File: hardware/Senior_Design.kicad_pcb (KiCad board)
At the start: 4 copper layers, 144 x 146 mm, 162 parts, among them IC301 TLV61220DBVT, J201 Conn_ARM_JTAG_SWD_10, J301 Barrel_Jack_Switch, J302 Conn_01x03, J401 Conn_ARM_JTAG_SWD_10, J601 USB_C_Receptacle_USB2.0_16P, J701 J0011D21BNL, Q301 CSD87503Q3E, Q302 CSD87503Q3E, Q303 Q_NMOS, SW201 SW_Push, SW401 SW_Push, U201 EFR32FG28A122F1024GM48-A, U202 USBLC6-2P6, U203 USBLC6-2P6, U301 TPS63020DSJR, U302 BQ25798RQMR, U401 USBLC6-2P6, U402 USBLC6-2P6, U403 BDE-MB1352P71UA32, U501 BME688, U502 USBLC6-2P6, U602 CDSOT236-0504C, U603 CP2102N-A02-GQFN20, U701 W5500, U702 USBLC6-2P6, U703 USBLC6-2P6, X201 HF_Crystal, Y201 LF_Crystal, Y701 25MHz

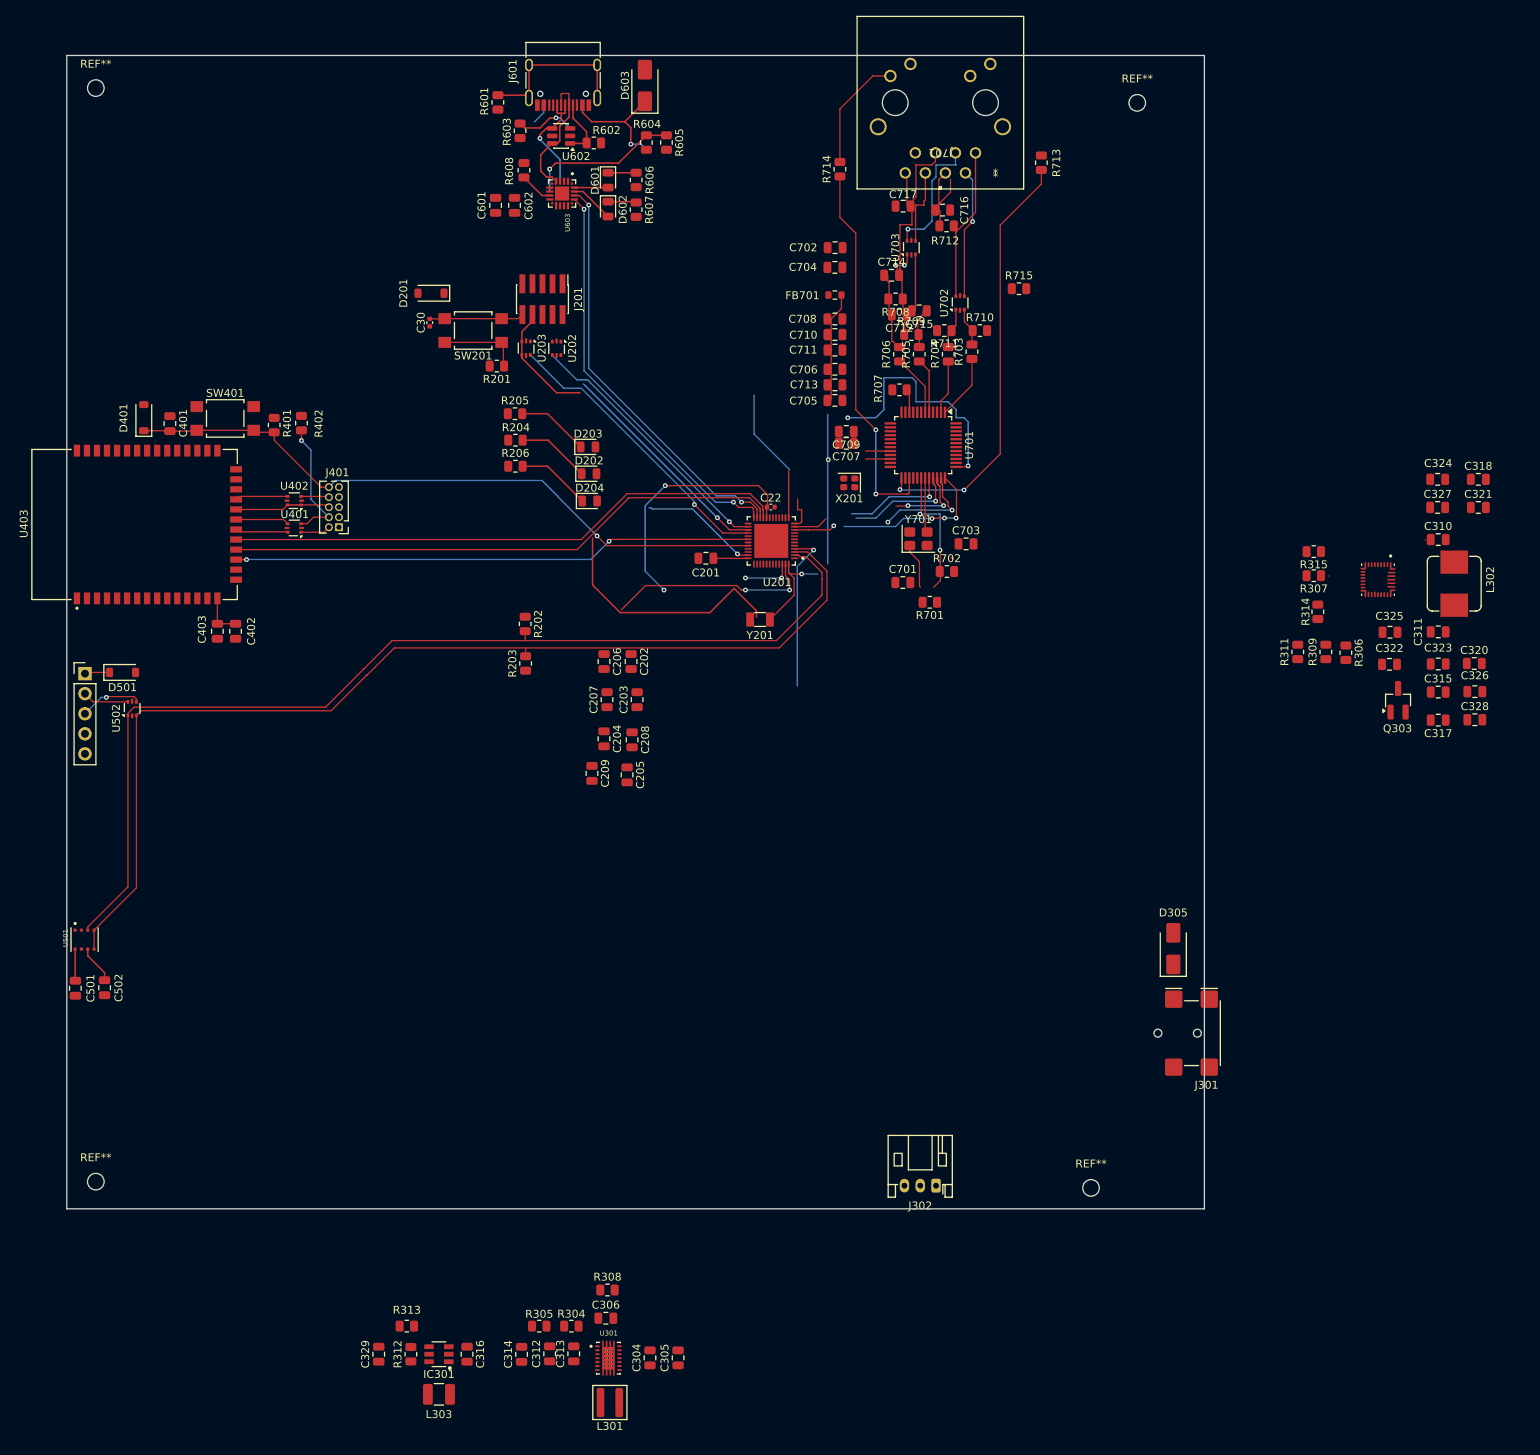
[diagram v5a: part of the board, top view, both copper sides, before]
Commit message: updated footprints
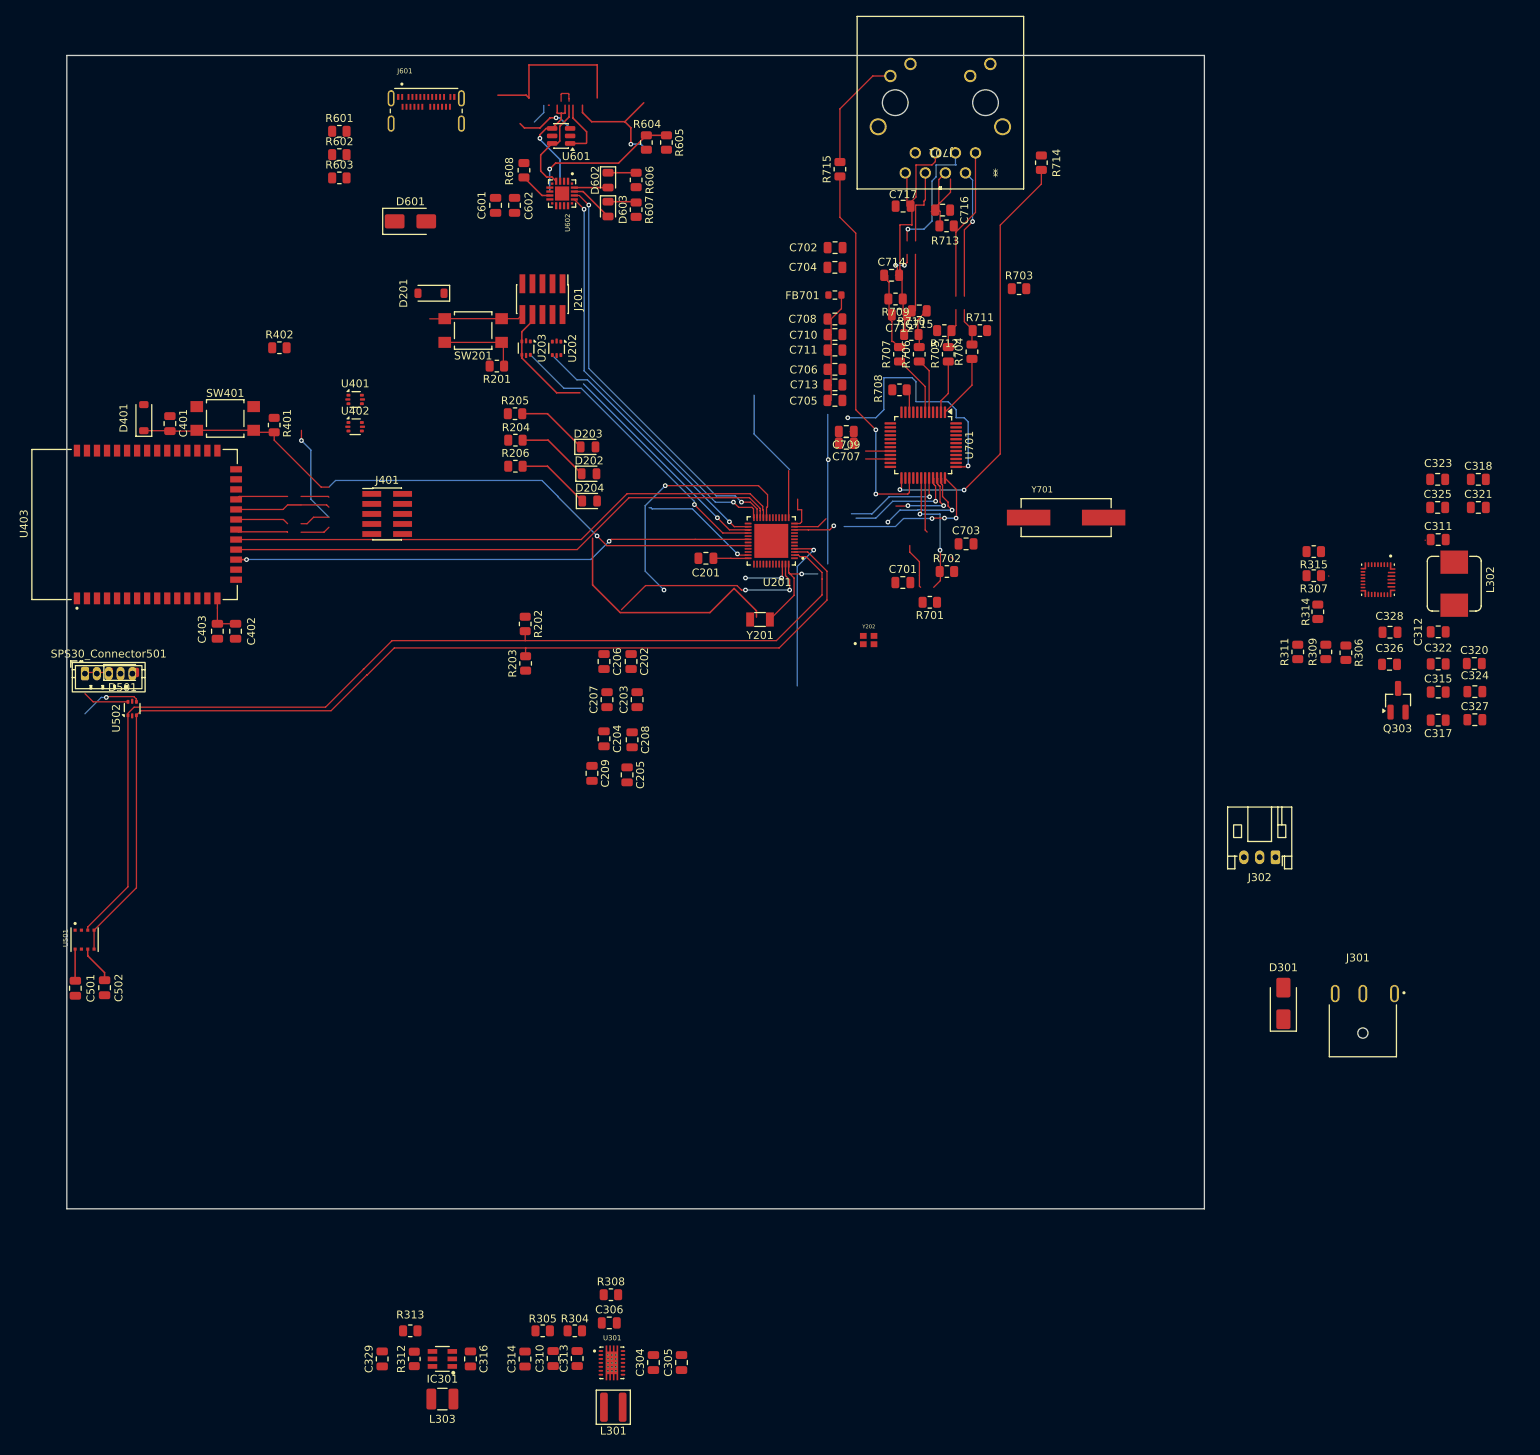
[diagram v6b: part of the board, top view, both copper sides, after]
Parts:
- removed C22: 120pF, Capacitor_SMD:C_0402_1005Metric
- removed C30: 100nF, Capacitor_SMD:C_0402_1005Metric
- removed the D603 at (96.2, 23.8)
- removed REF** (x4): MountingHole_2.1mm, MountingHole:MountingHole_2.1mm
- removed U702, U703: USBLC6-2P6, Package_TO_SOT_SMD:SOT-666
- removed X201: HF_Crystal, Crystal:Crystal_SMD_2016-4Pin_2.0x1.6mm
- added D601: SMAJ12A, Diode_SMD:D_SMA, F.Cu at (66.5, 41.0)
- added Y202: ECS-390-CDX-1932, pyronet_footprints:XTAL_ECS-390-CDX-1932, F.Cu at (124.5, 94.0)
- J301: value Barrel_Jack_Switch -> 54-00125; footprint Connector_BarrelJack:BarrelJack_Wuerth_694102107102_1.0x3.9mm -> pyronet_footprints:TENSILITY_54-00125
- J401: footprint Connector_PinHeader_1.27mm:PinHeader_2x05_P1.27mm_Vertical -> Connector_PinHeader_1.27mm:PinHeader_2x05_P1.27mm_Vertical_SMD
- J601: value USB_C_Receptacle_USB2.0_16P -> 2305018-2; footprint Connector_USB:USB_C_Receptacle_HRO_TYPE-C-31-M-12 -> pyronet_footprints:TE_2305018-2
- R601: value 1M -> 5.1k
- R602: value 5.1k -> 1M
- SPS30_Connector501: footprint Connector_PinHeader_2.54mm:PinHeader_1x05_P2.54mm_Vertical -> Connector_JST:JST_ZH_B5B-ZR_1x05_P1.50mm_Vertical
- Y701: value 25MHz -> ECS-250-18-5PX-F-TR; footprint Crystal:Crystal_SMD_3225-4Pin_3.2x2.5mm -> pyronet_footprints:XTAL_ECS-250-18-5PX-F-TR
- moved J302 59.8 mm to (176.0, 121.5)
- moved R602 32.2 mm to (57.5, 32.5)
- moved R603 23.6 mm to (57.5, 35.5), turned to 0 degrees
- moved J301 22.8 mm to (187.1, 143.8), turned to 0 degrees
- moved R601 20.4 mm to (57.5, 29.6), turned to 0 degrees
- moved Y701 18.9 mm to (149.5, 78.5)
- moved J601 18.5 mm to (68.5, 28.9), turned to 0 degrees
- moved U401 18.0 mm to (59.5, 63.5), turned to 0 degrees
- moved D301 15.6 mm to (177.0, 140.0)
- moved U402 12.1 mm to (59.5, 67.0), turned to 0 degrees
- moved R402 9.94 mm to (49.9, 57.0), turned to 0 degrees
- moved J401 6.33 mm to (63.5, 78.0), turned to 0 degrees
- moved C304 0.74 mm to (97.3, 185.5)
- moved C305 0.74 mm to (100.8, 185.5)
- moved C314 0.74 mm to (81.0, 185.0)
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- renumbered C312 to C310, C310 to C311, C311 to C312, C323 to C322, C324 to C323, C326 to C324, C327 to C325, C322 to C326, C328 to C327, C325 to C328, D305 to D301, D601 to D602, D602 to D603, R715 to R703, R703 to R704, R704 to R705, R705 to R706, R706 to R707, R707 to R708, R708 to R709, R709 to R710, R710 to R711, R711 to R712, R712 to R713, R713 to R714, R714 to R715, U602 to U601, U603 to U602
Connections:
- R601 pad 1: Net-(J601-SHIELD) -> GND
- R601 pad 2: GND -> /USB-C/CC1
- R602 pad 1: /USB-C/CC1 -> Net-(J601-SHIELD-PadSH1)
- Y701 pad 2: GND -> Net-(U701-XO)
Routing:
- net +3.3V: track 0.74 -> 32.4 mm, vias 0 -> 2
- net /MCU/PAVDD: track 31.6 -> 0.00 mm, vias 2 -> 0
- net Net-(J601-SHIELD): track 21.1 -> 0.00 mm
- net (no net): track 96.2 -> 117.3 mm
- net /MCU/nRST: track 80.5 -> 82.4 mm
- net Net-(U2-~{RESET}): track 1.91 -> 0.00 mm

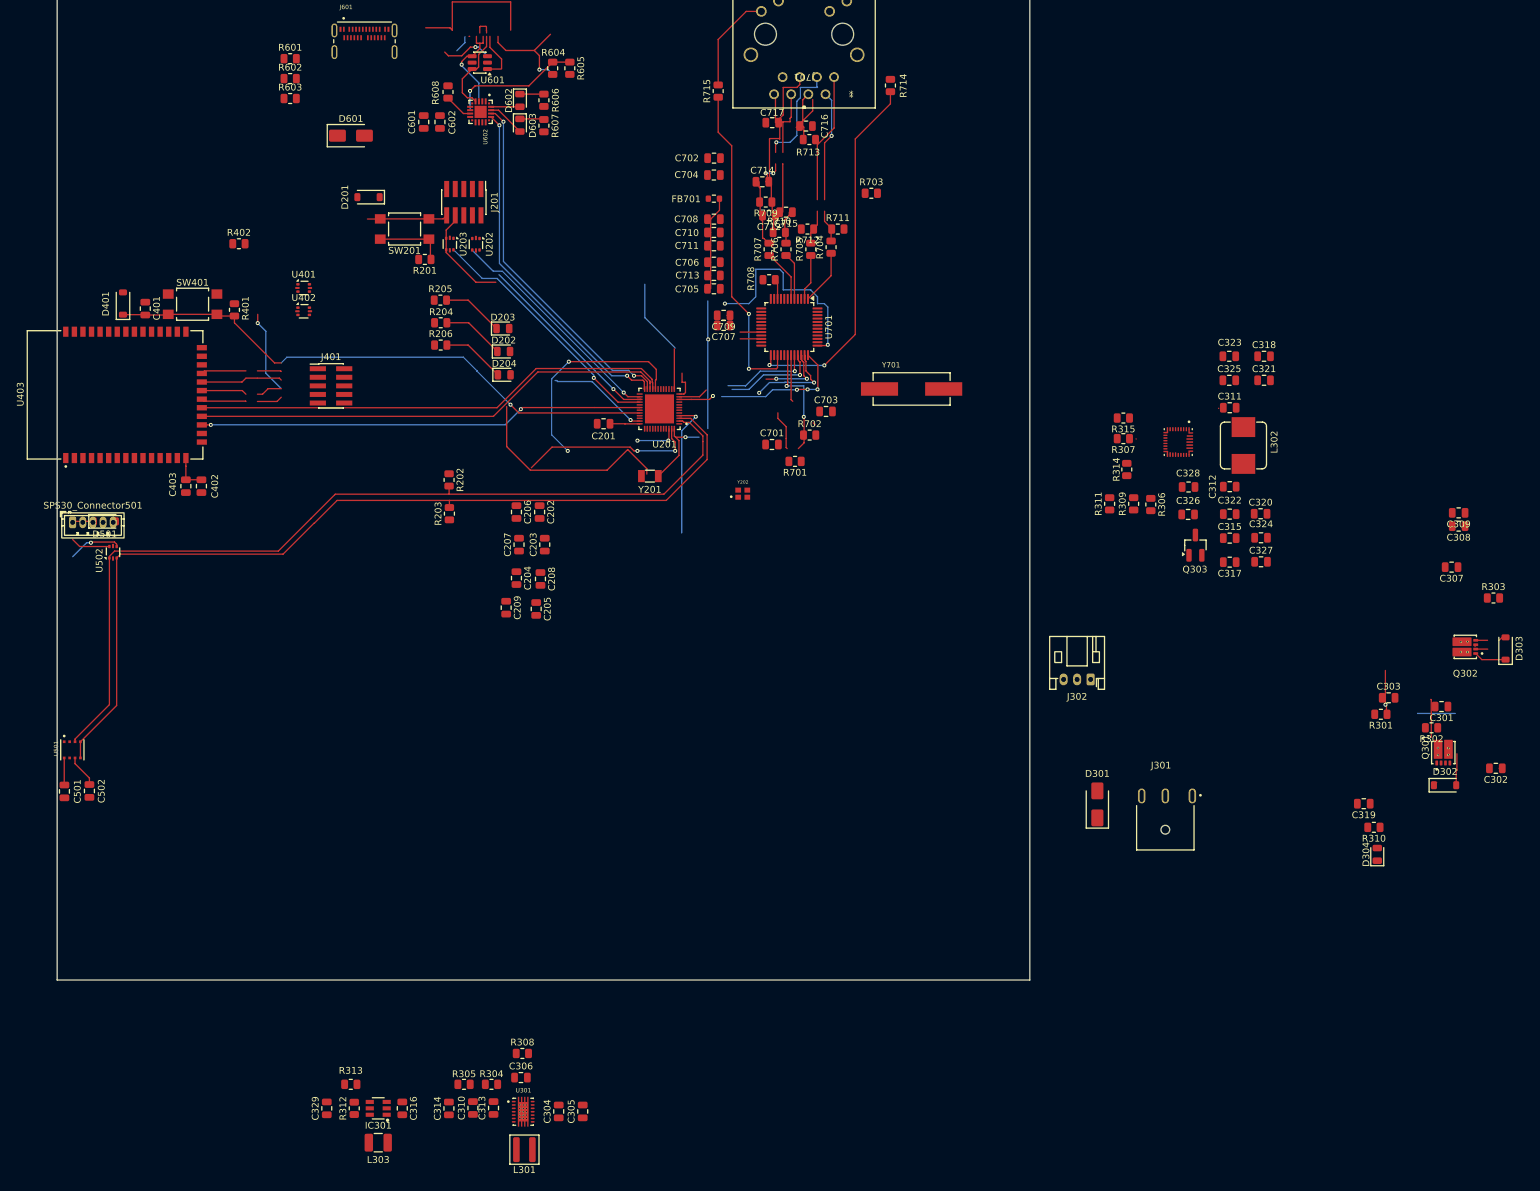
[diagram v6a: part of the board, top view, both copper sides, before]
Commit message: updated labels
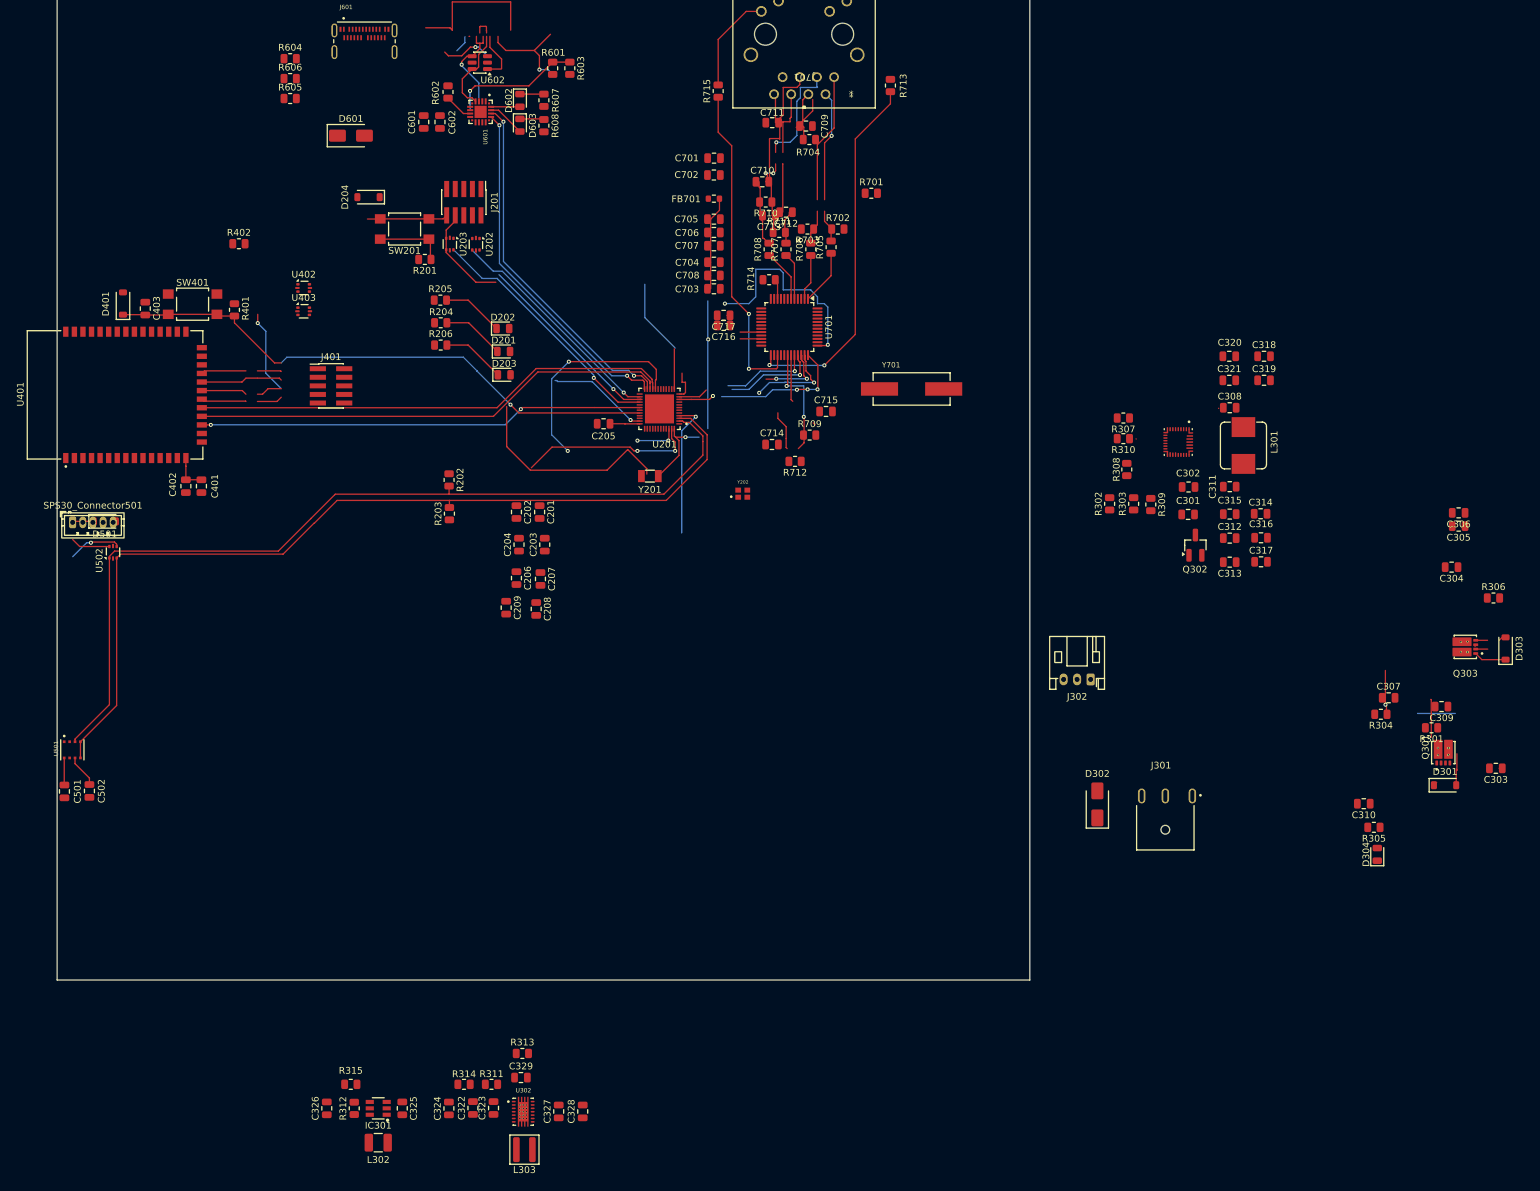
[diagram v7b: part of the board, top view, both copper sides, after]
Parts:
- renumbered C202 to C201, C206 to C202, C207 to C204, C201 to C205, C204 to C206, C208 to C207, C205 to C208, C326 to C301, C328 to C302, C302 to C303, C307 to C304, C308 to C305, C309 to C306, C303 to C307, C311 to C308, C301 to C309, C319 to C310, C312 to C311, C315 to C312, C317 to C313, C320 to C314, C322 to C315, C324 to C316, C327 to C317, C321 to C319, C323 to C320, C325 to C321, C310 to C322, C313 to C323, C314 to C324, C316 to C325, C329 to C326, C304 to C327, C305 to C328, C306 to C329, C402 to C401, C403 to C402, C401 to C403, C702 to C701, C704 to C702, C705 to C703, C706 to C704, C708 to C705, C710 to C706, C711 to C707, C713 to C708, C716 to C709, C714 to C710, C717 to C711, C715 to C712, C712 to C713, C701 to C714, C703 to C715, C707 to C716, C709 to C717, D202 to D201, D203 to D202, D204 to D203, D201 to D204, D302 to D301, D301 to D302, L302 to L301, L303 to L302, L301 to L303, Q303 to Q302, Q302 to Q303, R302 to R301, R311 to R302, R309 to R303, R301 to R304, R310 to R305, R303 to R306, R315 to R307, R314 to R308, R306 to R309, R307 to R310, R304 to R311, R308 to R313, R305 to R314, R313 to R315, R604 to R601, R608 to R602, R605 to R603, R601 to R604, R603 to R605, R602 to R606, R606 to R607, R607 to R608, R703 to R701, R711 to R702, R712 to R703, R713 to R704, R704 to R705, R705 to R706, R706 to R707, R707 to R708, R702 to R709, R709 to R710, R710 to R711, R701 to R712, R714 to R713, R708 to R714, U302 to U301, U301 to U302, U403 to U401, U401 to U402, U402 to U403, U602 to U601, U601 to U602
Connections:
- net /BMS/INT0 renamed /BMS/BQ_INT
- net /MCU/MCU_Debug renamed /MCU/DEBUG_LED3
- C403 pad 1: /MCU/BDE_RESET -> /Wi-SUN Module/BDE_RST
- D201 pad 2: /MCU/BME688_Degbug -> /MCU/DEBUG_LED1
- D202 pad 2: /MCU/SPS30_Debug -> /MCU/DEBUG_LED2
- D401 pad 1: /MCU/BDE_RESET -> /Wi-SUN Module/BDE_RST
- J401 pad 10: /MCU/BDE_RESET -> /Wi-SUN Module/BDE_RST
- R401 pad 2: /MCU/BDE_RESET -> /Wi-SUN Module/BDE_RST
- SW401 pad 2: /MCU/BDE_RESET -> /Wi-SUN Module/BDE_RST
- U201 pad 10: /Ethernet/INT1 -> /MCU/W5500_INT
- U201 pad 23: /MCU/DEBUG_UART_TX -> /MCU/MCU_TX_CP_RX
- U201 pad 24: /MCU/DEBUG_UART_RX -> /MCU/MCU_RX_CP_TX
- U201 pad 33: /MCU/SPS30_Debug -> /MCU/DEBUG_LED1
- U201 pad 34: /MCU/BME688_Degbug -> /MCU/DEBUG_LED2
- U201 pad 9: /MCU/nRST -> /MCU/W5500_RST
- U401 pad 30: /MCU/BDE_RESET -> /Wi-SUN Module/BDE_RST
- U601 pad 17: /MCU/DEBUG_UART_RX -> /MCU/MCU_TX_CP_RX
- U601 pad 18: /MCU/DEBUG_UART_TX -> /MCU/MCU_RX_CP_TX
- U701 pad 37: /MCU/nRST -> /Ethernet/W550_RST
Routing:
- net (no net): track 117.3 -> 182.6 mm, vias 2 -> 4
- net /MCU/DEBUG_UART_TX: track 52.8 -> 0.00 mm, vias 2 -> 0
- net /MCU/DEBUG_UART_RX: track 52.1 -> 0.00 mm, vias 2 -> 0
- net /Ethernet/RD+: track 16.4 -> 52.1 mm, vias 1 -> 3
- net /Ethernet/W550_RST: track 0.00 -> 31.3 mm, vias 0 -> 2
- net /MCU/nRST: track 82.4 -> 51.1 mm, vias 3 -> 1
- net /Wi-SUN Module/BDE_RST: track 0.00 -> 27.1 mm
- net /MCU/BDE_RESET: track 83.9 -> 56.9 mm
- net GND: track 0.00 -> 9.89 mm
- net Net-(C714-Pad1): track 5.87 -> 0.00 mm
- net /MCU/W5500_INT: track 0.00 -> 5.19 mm, vias 0 -> 1
- net /Ethernet/INT1: track 25.5 -> 20.3 mm, vias 4 -> 3
